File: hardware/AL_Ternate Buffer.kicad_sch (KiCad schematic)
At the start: 55 parts, among them J1 AudioJack3_Ground_Switch, J2 AudioJack3_Ground_Switch, J3 AudioJack3_Ground_Switch, J4 Barrel_Jack_MountingPin, SW1 SW_SPDT, U1 OPA1664AIDR

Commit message: Tentative schematic finish.
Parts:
- removed J4: Barrel_Jack_MountingPin, symbol Connector:Barrel_Jack_MountingPin
- removed R14, R16, R18, R23, R3: 10k, symbol Device:R_US
- added H1, H2, H3, H4: MountingHole_Pad, MountingHole:MountingHole_2.7mm_M2.5_Pad, symbol Mechanical:MountingHole_Pad
- added J1: FC68148, Connector_BarrelJack:BarrelJack_Horizontal, symbol Connector:Barrel_Jack_Switch
- added R15, R17, R20, R25, R5: 10k 0.5%, Resistor_SMD:R_0603_1608Metric_Pad0.98x0.95mm_HandSolder, symbol Device:R_US
- BT1: Part Number (none) -> 232-M
- C1, C2, C3, C6: value 47u -> 47u 35V 20%; footprint (none) -> Capacitor_SMD:C_2220_5750Metric_Pad1.97x5.40mm_HandSolder; Part Number (none) -> CGA9N1X7R1V476M230KC
- C10, C9: value 100p -> 100p 50V 5%; footprint (none) -> Capacitor_SMD:C_0805_2012Metric_Pad1.18x1.45mm_HandSolder; Part Number (none) -> GCM2165C1H101JA16D
- C11: value 100u -> 100n 100V 10%; footprint (none) -> Capacitor_SMD:C_0805_2012Metric_Pad1.18x1.45mm_HandSolder; Part Number (none) -> GCJ21BR72A104KA01L
- C12: value 100u -> 100n 100V 10%; footprint (none) -> Capacitor_SMD:C_0805_2012Metric_Pad1.18x1.45mm_HandSolder; Part Number (none) -> GCJ21BR72A104KA01L; now not fitted
- C13, C14, C15, C16, C4, C7: value 10u -> 10u 25V 10%; footprint (none) -> Capacitor_SMD:C_0805_2012Metric_Pad1.18x1.45mm_HandSolder; Part Number (none) -> GRT21BC71E106KE13L
- C17, C18: value 10u -> 10u 75V 10%; footprint (none) -> Capacitor_SMD:C_1210_3225Metric_Pad1.33x2.70mm_HandSolder; Part Number (none) -> CGA6P1X7R1N106K250AC
- C5, C8: value 1u -> 1u 50V 10%; footprint (none) -> Capacitor_SMD:C_0805_2012Metric_Pad1.18x1.45mm_HandSolder; Part Number (none) -> GCM21BR71H105KA03L
- D1, D2: footprint (none) -> Diode_SMD:D_SMB-SMC_Universal_Handsoldering; Part Number (none) -> S3GHE3_A/I
- D3: value LED -> QBL8IW60D-NW; footprint (none) -> LED_THT:LED_D5.0mm; Part Number (none) -> QBL8IW60D-NW
- J2: renamed from J1; value AudioJack3_Ground_Switch -> NMJ6HCD2; footprint (none) -> Connector_Audio:Jack_6.35mm_Neutrik_NMJ6HCD2_Horizontal; Part Number (none) -> NMJ6HCD2
- J3: renamed from J2; value AudioJack3_Ground_Switch -> NMJ6HCD2; footprint (none) -> Connector_Audio:Jack_6.35mm_Neutrik_NMJ6HCD2_Horizontal; Part Number (none) -> NMJ6HCD2
- J4: renamed from J3; value AudioJack3_Ground_Switch -> NMJ6HCD2; footprint (none) -> Connector_Audio:Jack_6.35mm_Neutrik_NMJ6HCD2_Horizontal; Part Number (none) -> NMJ6HCD2
- R1: renamed from R25; footprint (none) -> Resistor_SMD:R_0603_1608Metric_Pad0.98x0.95mm_HandSolder; Part Number (none) -> 560112116101
- R10: renamed from R9; value 1M -> 1M 1%; footprint (none) -> Resistor_SMD:R_0603_1608Metric_Pad0.98x0.95mm_HandSolder; Part Number (none) -> RCA06031M00FKEASR
- R11: renamed from R10; value 1k -> 1k 1%; footprint (none) -> Resistor_SMD:R_0603_1608Metric_Pad0.98x0.95mm_HandSolder; Part Number (none) -> RCA06031K00FKEASR
- R12: renamed from R11; value 1k -> 1k 1%; footprint (none) -> Resistor_SMD:R_0603_1608Metric_Pad0.98x0.95mm_HandSolder; Part Number (none) -> RCA06031K00FKEASR
- R13: renamed from R12; value 1M -> 1M 1%; footprint (none) -> Resistor_SMD:R_0603_1608Metric_Pad0.98x0.95mm_HandSolder; Part Number (none) -> RCA06031M00FKEASR
- R14: renamed from R13; value 10k -> 10k 0.5%; footprint (none) -> Resistor_SMD:R_0603_1608Metric_Pad0.98x0.95mm_HandSolder; Part Number (none) -> CRCW060310K0DKEAHP
- R16: renamed from R15; value 10k -> 10k 0.5%; footprint (none) -> Resistor_SMD:R_0603_1608Metric_Pad0.98x0.95mm_HandSolder; Part Number (none) -> CRCW060310K0DKEAHP
- R18: renamed from R17; footprint (none) -> Resistor_SMD:R_0603_1608Metric_Pad0.98x0.95mm_HandSolder; Part Number (none) -> 560112116001
- R19, R24, R4: value 10k -> 10k 0.5%; footprint (none) -> Resistor_SMD:R_0603_1608Metric_Pad0.98x0.95mm_HandSolder; Part Number (none) -> CRCW060310K0DKEAHP
- R2: renamed from R1; value 100 -> 100 5%; footprint (none) -> Resistor_SMD:R_0603_1608Metric_Pad0.98x0.95mm_HandSolder; Part Number (none) -> RMCA0603JT100R-HP
- R21: renamed from R20; footprint (none) -> Resistor_SMD:R_0603_1608Metric_Pad0.98x0.95mm_HandSolder; Part Number (none) -> 560112116001
- R22: renamed from R21; value 10k -> 10k 0.5%; footprint (none) -> Resistor_SMD:R_0603_1608Metric_Pad0.98x0.95mm_HandSolder; Part Number (none) -> CRCW060310K0DKEAHP
- R23: renamed from R22; value 10k -> 10k 0.5%; footprint (none) -> Resistor_SMD:R_0603_1608Metric_Pad0.98x0.95mm_HandSolder; Part Number (none) -> CRCW060310K0DKEAHP
- R3: renamed from R2; value 100 -> 100 5%; footprint (none) -> Resistor_SMD:R_0603_1608Metric_Pad0.98x0.95mm_HandSolder; Part Number (none) -> RMCA0603JT100R-HP
- R6: renamed from R5; value 10k -> 10k 0.5%; footprint (none) -> Resistor_SMD:R_0603_1608Metric_Pad0.98x0.95mm_HandSolder; Part Number (none) -> CRCW060310K0DKEAHP
- R7: renamed from R6; value 10k -> 10k 0.5%; footprint (none) -> Resistor_SMD:R_0603_1608Metric_Pad0.98x0.95mm_HandSolder; Part Number (none) -> CRCW060310K0DKEAHP
- R8: renamed from R7; value 1k -> 1k 1%; footprint (none) -> Resistor_SMD:R_0603_1608Metric_Pad0.98x0.95mm_HandSolder; Part Number (none) -> RCA06031K00FKEASR
- R9: renamed from R8; value 1k -> 1k 1%; footprint (none) -> Resistor_SMD:R_0603_1608Metric_Pad0.98x0.95mm_HandSolder; Part Number (none) -> RCA06031K00FKEASR
- RV1, RV2: value 10k C -> 10k A; footprint (none) -> Potentiometer_THT:Potentiometer_Runtron_RM-065_Vertical; Part Number (none) -> PT6KV-103A2020
- SW1: value SW_SPDT -> 7101SYZQE; footprint (none) -> Connector_PinHeader_2.54mm:PinHeader_1x03_P2.54mm_Vertical; Part Number (none) -> 7101SYZQE
- U1: Part Number (none) -> OPA1664AIDR
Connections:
- net GND: now also R19.2, H1.1, H2.1, H3.1, H4.1, J1.1, R25.2
- net OUT 1 - MONO: now also R19.1
- net OUT 2 - MONO: now also R25.1; no longer R24.1
- net OUT 2 - STEREO: now also R24.1
- net VIN: now also J1.2
- net at R11.2, U1.5 (+): now also R15.1
- net at C15.1, C16.1, U1.7: now also R15.2
- net at C14.2: now also R17.1
- net at R22.1, U1.12 (+): now also R17.2
- net at C3.1, C9.2, R10.2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: now also R4.2
- net at R23.1, U1.10 (+): now also R20.2; no longer R19.2
- net at C10.2, C6.1, R13.2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: now also R5.2; no longer R4.2
- net at C2.1, R3.2: now also R5.1; no longer R4.1
- net at C16.2: now also R20.1; no longer R19.1
- net at C1.1, R2.2: now also R4.1
- no-connect marks 0 -> 1
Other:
- moved on the sheet: C11, U1E

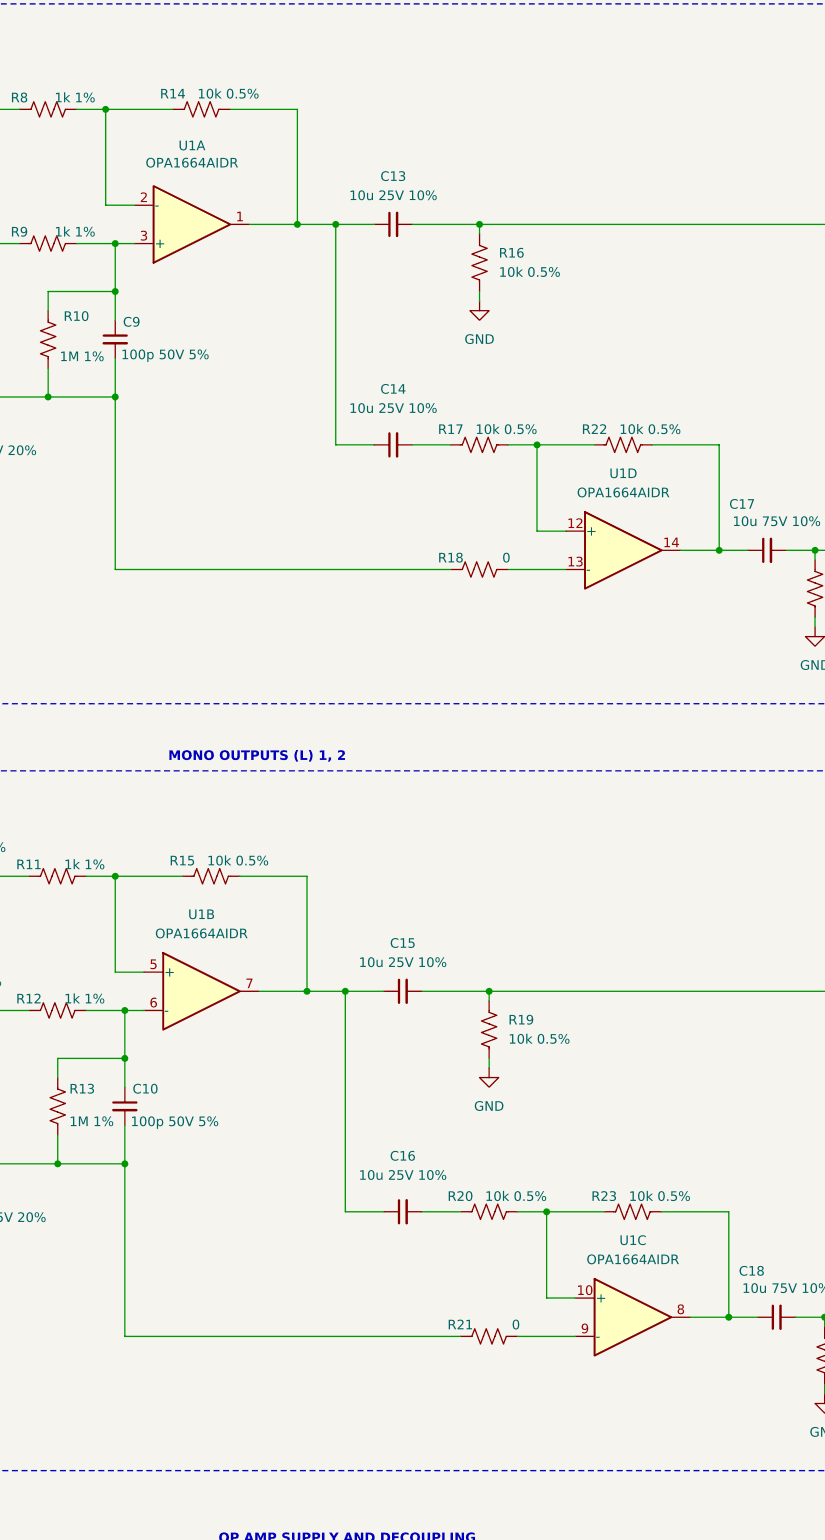
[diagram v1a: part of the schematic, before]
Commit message: Caught error regarding op-amp polarity. Partial routing/placement progress.
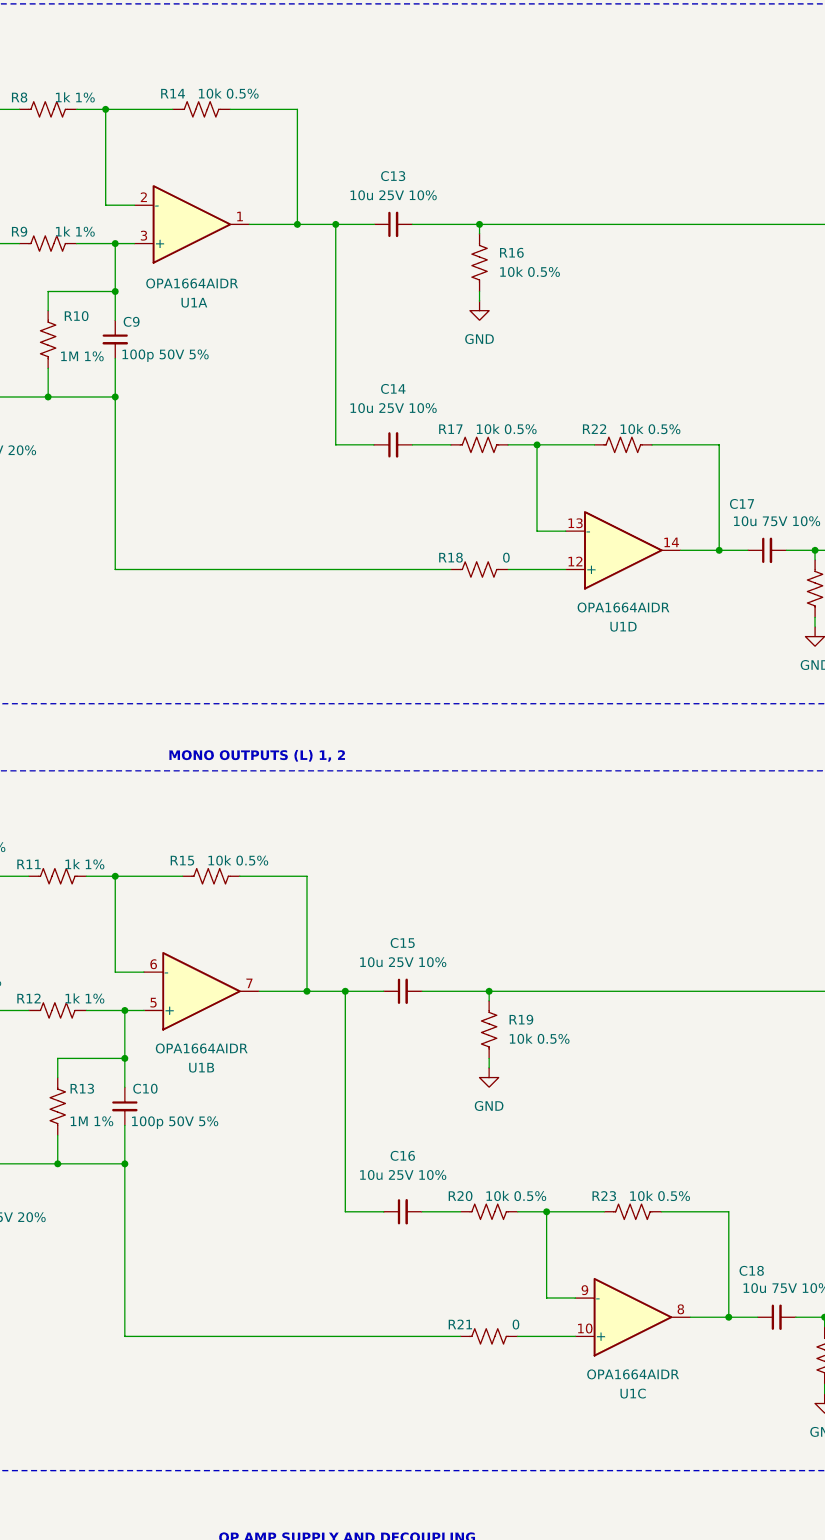
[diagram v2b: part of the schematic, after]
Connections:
- net at R17.2, R22.1: now also U1.13 (-); no longer U1.12 (+)
- net at R20.2, R23.1: now also U1.9 (-); no longer U1.10 (+)
- net at R11.2, R15.1: now also U1.6 (-); no longer U1.5 (+)
- net at C10.1, R12.2, R13.1: now also U1.5 (+); no longer U1.6 (-)
- net at R18.2: now also U1.12 (+); no longer U1.13 (-)
- net at R21.2: now also U1.10 (+); no longer U1.9 (-)
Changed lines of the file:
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@@
 		(lib_id "Amplifier_Operational:OPA1664D")
 		(at 241.3 96.52 0)
+		(mirror x)
 		(unit 4)
 		(body_style 1)
@@
 		(in_pos_files yes)
 		(dnp no)
-		(fields_autoplaced yes)
 		(property "Reference" "U1"
-			(at 241.3 86.36 0)
+			(at 241.3 106.68 0)
 			(show_name no)
 			(do_not_autoplace no)
@@
 		)
 		(property "Value" "OPA1664AIDR"
-			(at 241.3 88.9 0)
+			(at 241.3 104.14 0)
 			(show_name no)
 			(do_not_autoplace no)
@@
 		)
 		(property "Footprint" "Package_SO:SOIC-14_3.9x8.7mm_P1.27mm"
-			(at 240.03 93.98 0)
+			(at 240.03 99.06 0)
 			(hide yes)
 			(show_name no)
@@
 		)
 		(property "Datasheet" "https://www.ti.com/lit/ds/symlink/opa1664.pdf"
-			(at 242.57 91.44 0)
+			(at 242.57 101.6 0)
 			(hide yes)
 			(show_name no)
@@
 		(dnp no)
 		(property "Reference" "U1"
-			(at 184.15 42.926 0)
+			(at 184.404 63.754 0)
 			(show_name no)
 			(do_not_autoplace no)
@@
 		)
 		(property "Value" "OPA1664AIDR"
-			(at 184.15 45.212 0)
+			(at 184.15 61.214 0)
 			(show_name no)
 			(do_not_autoplace no)
@@
 		(lib_id "Amplifier_Operational:OPA1664D")
 		(at 185.42 154.94 0)
+		(mirror x)
 		(unit 2)
 		(body_style 1)
@@
 		(in_pos_files yes)
 		(dnp no)
-		(fields_autoplaced yes)
 		(property "Reference" "U1"
-			(at 185.42 144.78 0)
+			(at 185.42 165.1 0)
 			(show_name no)
 			(do_not_autoplace no)
@@
 		)
 		(property "Value" "OPA1664AIDR"
-			(at 185.42 147.32 0)
+			(at 185.42 162.56 0)
 			(show_name no)
 			(do_not_autoplace no)
@@
 		)
 		(property "Footprint" "Package_SO:SOIC-14_3.9x8.7mm_P1.27mm"
-			(at 184.15 152.4 0)
+			(at 184.15 157.48 0)
 			(hide yes)
 			(show_name no)
@@
 		)
 		(property "Datasheet" "https://www.ti.com/lit/ds/symlink/opa1664.pdf"
-			(at 186.69 149.86 0)
+			(at 186.69 160.02 0)
 			(hide yes)
 			(show_name no)
@@
 		(lib_id "Amplifier_Operational:OPA1664D")
 		(at 242.57 198.12 0)
+		(mirror x)
 		(unit 3)
 		(body_style 1)
@@
 		(in_pos_files yes)
 		(dnp no)
-		(fields_autoplaced yes)
 		(property "Reference" "U1"
-			(at 242.57 187.96 0)
+			(at 242.57 208.28 0)
 			(show_name no)
 			(do_not_autoplace no)
@@
 		)
 		(property "Value" "OPA1664AIDR"
-			(at 242.57 190.5 0)
+			(at 242.57 205.74 0)
 			(show_name no)
 			(do_not_autoplace no)
@@
 		)
 		(property "Footprint" "Package_SO:SOIC-14_3.9x8.7mm_P1.27mm"
-			(at 241.3 195.58 0)
+			(at 241.3 200.66 0)
 			(hide yes)
 			(show_name no)
@@
 		)
 		(property "Datasheet" "https://www.ti.com/lit/ds/symlink/opa1664.pdf"
-			(at 243.84 193.04 0)
+			(at 243.84 203.2 0)
 			(hide yes)
 			(show_name no)

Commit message: Finished tentative routing.
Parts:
- removed H1, H2, H3, H4: MountingHole_Pad, MountingHole:MountingHole_2.7mm_M2.5_Pad, symbol Mechanical:MountingHole_Pad
